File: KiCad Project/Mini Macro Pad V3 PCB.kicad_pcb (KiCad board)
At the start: 4 copper layers, 65 x 65 mm, 98 parts, among them J1 USB_C_Receptacle_USB2.0_14P, SW1 SW_Push bootsel, SW10 SW_Push, SW11 SW_Push, SW12 SW_Push, SW13 SW_Push, SW14 SW_Push, SW15 SW_Push, SW16 SW_Push, SW17 SW_Push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

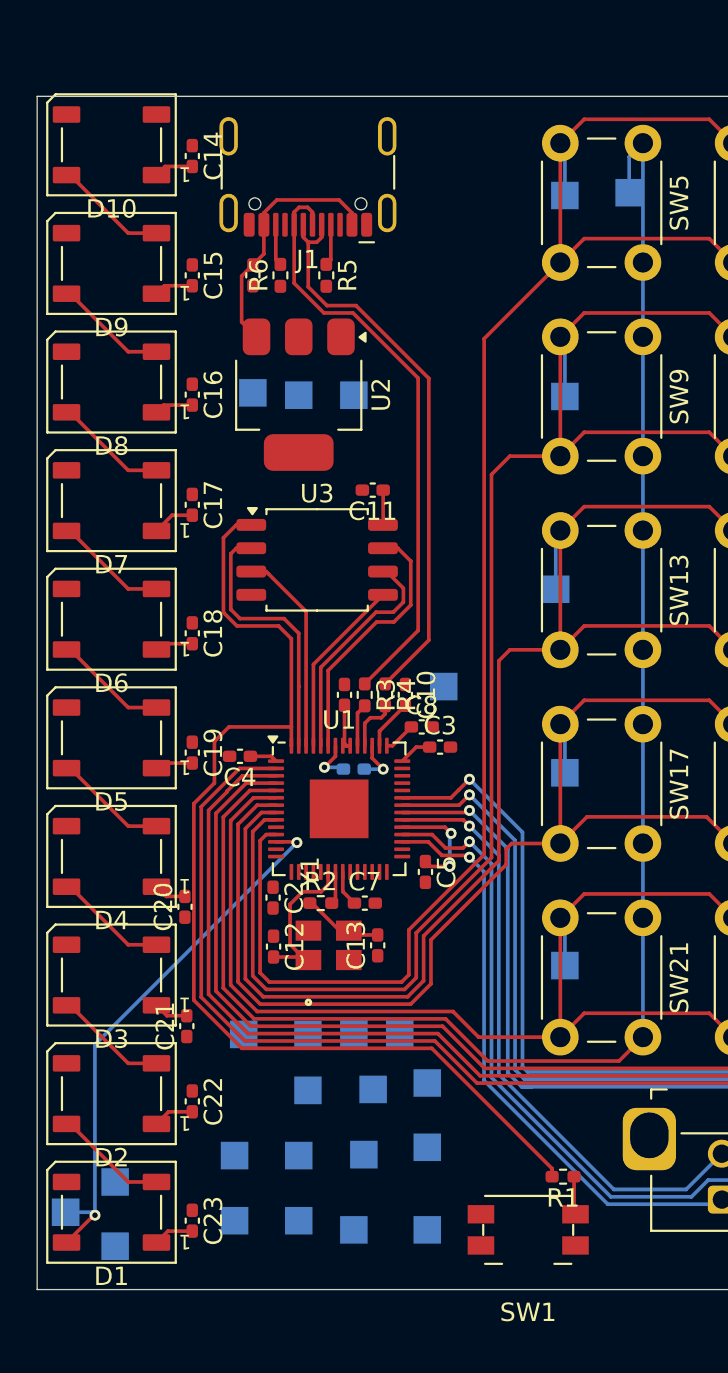
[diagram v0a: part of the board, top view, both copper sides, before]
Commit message: added vias to connect components to ground & power planes
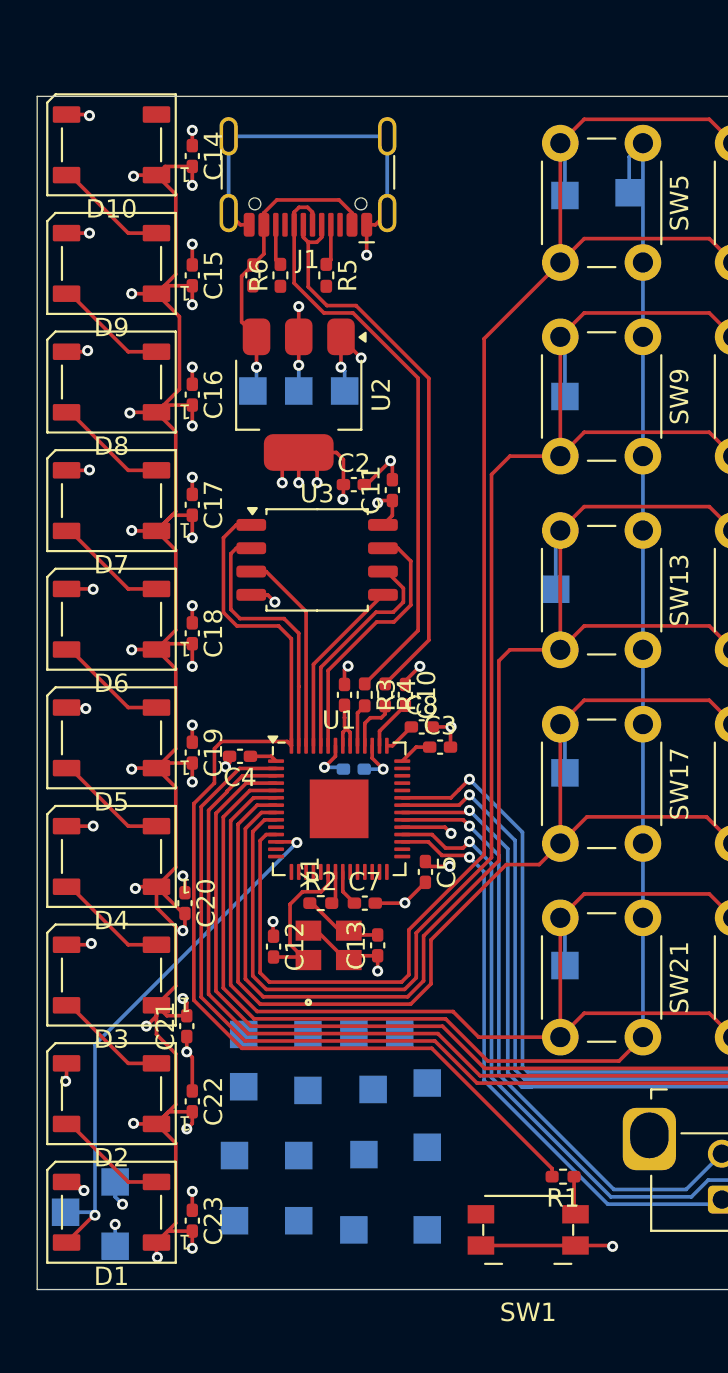
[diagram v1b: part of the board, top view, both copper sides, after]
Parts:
- moved TP14 24.4 mm to (114.0, 111.2)
- moved C2 22.9 mm to (120.0, 78.4), turned to 0 degrees
- moved C11 1.07 mm to (122.1, 78.7), turned to 90 degrees
- moved TP21 0.55 mm to (119.5, 73.3)
- moved TP20 0.23 mm to (117.0, 73.3)
- moved C20 0.20 mm to (110.8, 101.2), turned to -90 degrees
- moved TP22 0.10 mm to (114.5, 73.3)
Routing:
- net +3.3V: track 37.9 -> 143.2 mm, vias 2 -> 31
- net GND: track 0.00 -> 74.1 mm, vias 0 -> 32
- net VBUS: track 13.6 -> 16.7 mm, vias 0 -> 1

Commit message: more routing work
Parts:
- removed TP10, TP11, TP12, TP7, TP8, TP9: ~, TestPoint:TestPoint_Pad_1.5x1.5mm
- C9: moved to F.Cu
- moved TP16 31.3 mm to (123.2, 88.7), turned to -90 degrees
- moved TP15 27.2 mm to (120.5, 88.7), turned to -90 degrees
- moved TP14 22.8 mm to (117.7, 88.7), turned to -90 degrees
- moved TP13 19.7 mm to (115.0, 88.7), turned to -90 degrees
- moved TP5 15.6 mm to (113.2, 101.2), turned to -90 degrees
- moved TP6 15.4 mm to (113.2, 103.5), turned to -90 degrees
- moved TP4 14.8 mm to (113.2, 98.8), turned to -90 degrees
- moved TP3 13.6 mm to (113.2, 96.5), turned to -90 degrees
- moved TP1 5.11 mm to (123.7, 105.9), turned to 90 degrees
- moved TP2 4.95 mm to (123.7, 103.5), turned to 90 degrees
- moved C9 4.17 mm to (119.0, 89.9), turned to 90 degrees
- moved C8 1.00 mm to (124.7, 91.6)
- moved R3 0.61 mm to (121.2, 89.9)
- moved C10 0.61 mm to (123.4, 89.9)
- moved C6 0.61 mm to (120.1, 89.9)
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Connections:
- U1 pad 17: Net-(U1-GPIO14) -> unconnected-(U1-GPIO14-Pad17)
- U1 pad 18: Net-(U1-GPIO15) -> unconnected-(U1-GPIO15-Pad18)
- U1 pad 26: unconnected-(U1-RUN-Pad26) -> +3.3V
- U1 pad 27: Net-(U1-GPIO16) -> unconnected-(U1-GPIO16-Pad27)
- U1 pad 28: Net-(U1-GPIO17) -> unconnected-(U1-GPIO17-Pad28)
- U1 pad 29: Net-(U1-GPIO18) -> unconnected-(U1-GPIO18-Pad29)
- U1 pad 30: Net-(U1-GPIO19) -> unconnected-(U1-GPIO19-Pad30)
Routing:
- net Net-(U1-GPIO27_ADC1): track 0.00 -> 11.5 mm, vias 0 -> 1
- net Net-(U1-GPIO26_ADC0): track 0.00 -> 11.1 mm, vias 0 -> 1
- net Net-(U1-SWCLK): track 0.00 -> 10.9 mm, vias 0 -> 1
- net Net-(U1-SWD): track 0.00 -> 10.7 mm, vias 0 -> 1
- net Net-(U1-GPIO13): track 0.00 -> 9.97 mm, vias 0 -> 1
- net Net-(C9-Pad1): track 2.36 -> 11.4 mm, vias 1 -> 2
- net /NEOPIXEL_DIN: track 29.8 -> 38.7 mm
- net Net-(U1-GPIO28_ADC2): track 0.00 -> 6.78 mm, vias 0 -> 1
- net GND: track 74.1 -> 80.3 mm, vias 32 -> 35
- net Net-(U1-VREG_VOUT): track 2.56 -> 8.77 mm, vias 1 -> 2
- net Net-(U1-GPIO29_ADC3): track 0.00 -> 6.17 mm, vias 0 -> 1
- net Net-(U1-GPIO10): track 0.00 -> 6.06 mm, vias 0 -> 1
- net +3.3V: track 143.2 -> 147.7 mm, vias 31 -> 32
- net Net-(U1-GPIO12): track 0.00 -> 4.08 mm, vias 0 -> 1
- net /MATRIX_R1: track 131.0 -> 134.5 mm
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
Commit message: test
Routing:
- net (no net): track 0.00 -> 26.9 mm, vias 0 -> 2
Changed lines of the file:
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@@
 	)
 	(segment
+		(start 164.9 113)
+		(end 163.5 113)
+		(width 0.2)
+		(layer "F.Cu")
+		(net 0)
+	)
+	(segment
+		(start 136.55 113.4)
+		(end 136.1 113.85)
+		(width 0.2)
+		(layer "F.Cu")
+		(net 0)
+	)
+	(segment
+		(start 153.7 113)
+		(end 152.85 113.85)
+		(width 0.2)
+		(layer "F.Cu")
+		(net 0)
+	)
+	(segment
+		(start 148.95 113.85)
+		(end 149 113.85)
+		(width 0.2)
+		(layer "F.Cu")
+		(net 0)
+	)
+	(segment
+		(start 148.5 113.4)
+		(end 148.95 113.85)
+		(width 0.2)
+		(layer "F.Cu")
+		(net 0)
+	)
+	(segment
+		(start 146.8 113.4)
+		(end 136.55 113.4)
+		(width 0.2)
+		(layer "F.Cu")
+		(net 0)
+	)
+	(segment
+		(start 146.8 113.4)
+		(end 148.5 113.4)
+		(width 0.2)
+		(layer "F.Cu")
+		(net 0)
+	)
+	(segment
+		(start 165.75 113.85)
+		(end 164.9 113)
+		(width 0.2)
+		(layer "F.Cu")
+		(net 0)
+	)
+	(segment
+		(start 163.5 113)
+		(end 153.7 113)
+		(width 0.2)
+		(layer "F.Cu")
+		(net 0)
+	)
+	(via micro
+		(at 146.8 113.4)
+		(size 0.6)
+		(drill 0.3)
+		(layers "F.Cu" "In1.Cu")
+		(net 0)
+	)
+	(via micro
+		(at 163.5 113)
+		(size 0.6)
+		(drill 0.3)
+		(layers "F.Cu" "In1.Cu")
+		(net 0)
+	)
+	(segment
 		(start 105.794445 97.005555)
 		(end 105.8 97)
@@
 	)
 	(segment
-		(start 117.5765 112.7804)
-		(end 127.9196 112.7804)
-		(width 0.2)
-		(layer "F.Cu")
-		(net 58)
-	)
-	(segment
 		(start 112.407912 94.657888)
-		(end 111.285863 95.779937)
-		(width 0.2)
-		(layer "F.Cu")
-		(net 58)
-	)
-	(segment
-		(start 112.8 92.392088)
 		(end 112.407912 92.784176)
 		(width 0.2)
@@
 	)
 	(segment
-		(start 111.285863 106.489763)
-		(end 117.5765 112.7804)
+		(start 113.600001 80.595)
+		(end 112.898 81.297001)
 		(width 0.2)
 		(layer "F.Cu")
@@
 	)
 	(segment
-		(start 113.600001 80.595)
-		(end 112.898 81.297001)
+		(start 116.2011 111.405)
+		(end 111.285863 106.489763)
 		(width 0.2)
 		(layer "F.Cu")
@@
 	)
 	(segment
-		(start 127.9196 112.7804)
-		(end 130.8025 115.6633)
+		(start 130.8025 116.1)
+		(end 130.8025 115.7075)
 		(width 0.2)
 		(layer "F.Cu")
@@
 	)
 	(segment
-		(start 116.367088 92.392088)
-		(end 112.8 92.392088)
+		(start 111.285863 95.779937)
+		(end 112.407912 94.657888)
 		(width 0.2)
 		(layer "F.Cu")
@@
 	(segment
 		(start 112.407912 92.784176)
-		(end 112.407912 94.657888)
+		(end 112.8 92.392088)
 		(width 0.2)
 		(layer "F.Cu")
@@
 	)
 	(segment
-		(start 116.6 92.625)
-		(end 116.367088 92.392088)
+		(start 111.285863 106.489763)
+		(end 111.285863 95.779937)
 		(width 0.2)
 		(layer "F.Cu")
@@
 	)
 	(segment
-		(start 111.285863 95.779937)
-		(end 111.285863 106.489763)
+		(start 116.367088 92.392088)
+		(end 116.6 92.625)
 		(width 0.2)
 		(layer "F.Cu")
@@
 	)
 	(segment
+		(start 126.5 111.405)
+		(end 116.2011 111.405)
+		(width 0.2)
+		(layer "F.Cu")
+		(net 58)
+	)
+	(segment
 		(start 113.7339 87.201)
 		(end 115.5339 87.201)
@@
 	)
 	(segment
-		(start 130.8025 115.6633)
-		(end 130.8025 116.1)
+		(start 112.8 92.392088)
+		(end 116.367088 92.392088)
 		(width 0.2)
 		(layer "F.Cu")
@@
 		(net 58)
 	)
+	(segment
+		(start 130.8025 115.7075)
+		(end 126.5 111.405)
+		(width 0.2)
+		(layer "F.Cu")
+		(net 58)
+	)
+	(zone
+		(net 0)
+		(net_name "")
+		(layer "F.Cu")
+		(name "$teardrop_padvia$")
+		(hatch none 0.1)
+		(priority 30000)
+		(attr
+			(teardrop
+				(type padvia)
+			)
+		)
+		(connect_pads yes
+			(clearance 0)
+		)
+		(min_thickness 0.0254)
+		(filled_areas_thickness no)
+		(fill yes
+			(thermal_gap 0.5)
+			(thermal_bridge_width 0.5)
+			(island_removal_mode 1)
+			(island_area_min 10)
+		)
+		(polygon
+			(pts
+				(xy 138.55 113.5) (xy 138.55 113.3) (xy 137.363555 112.601115) (xy 136.099 113.85) (xy 137.55 114.600312)
+			)
+		)
+	)
 	(zone

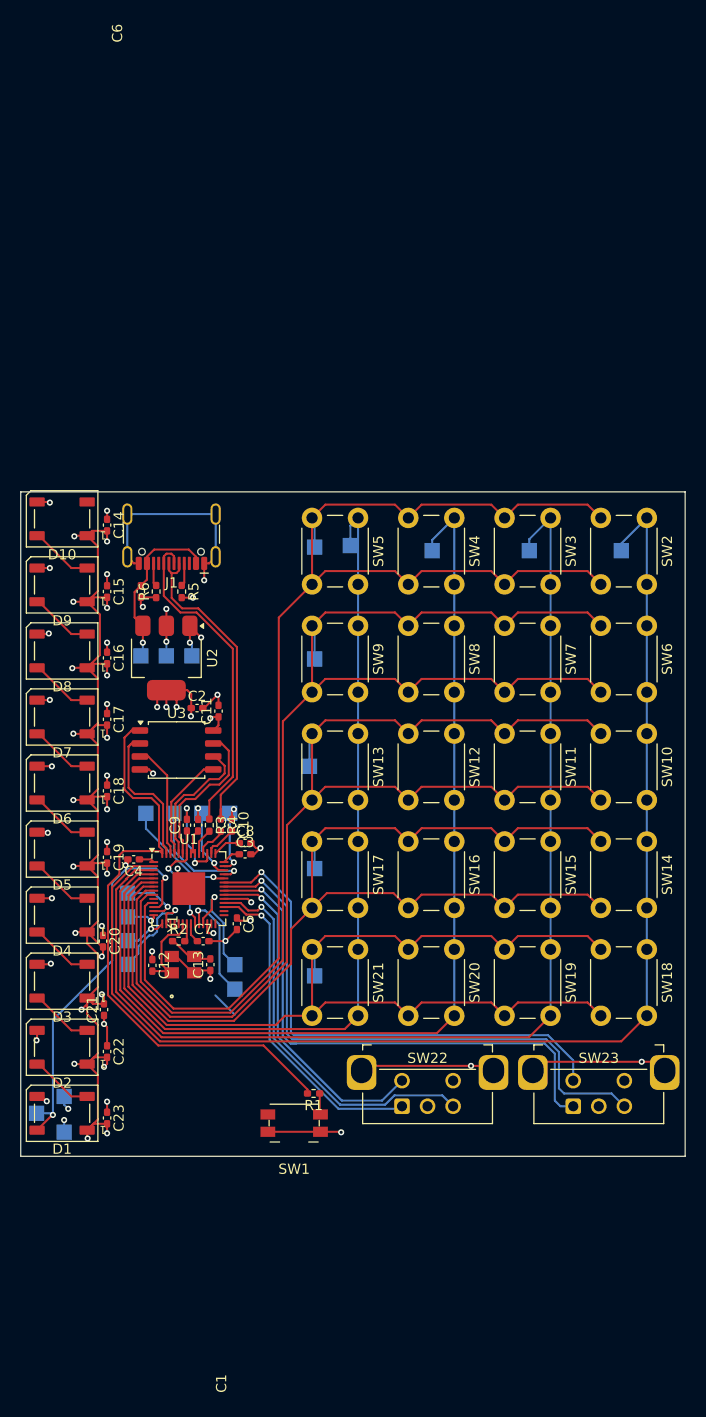
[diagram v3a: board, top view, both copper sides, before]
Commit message: tweaks for DRC
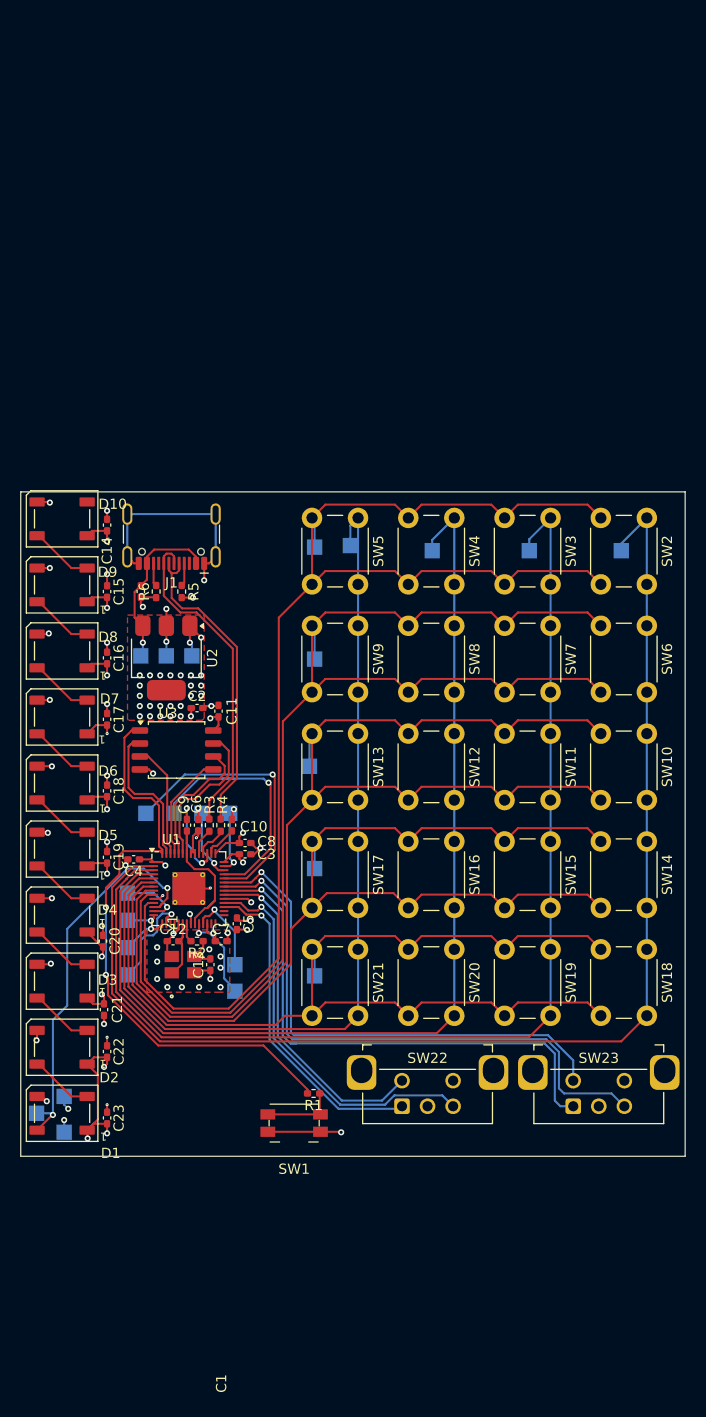
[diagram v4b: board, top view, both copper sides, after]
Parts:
- U1: footprint Package_DFN_QFN:QFN-56-1EP_7x7mm_P0.4mm_EP3.2x3.2mm -> Package_DFN_QFN:QFN-56-1EP_7x7mm_P0.4mm_EP3.2x3.2mm_ThermalVias
- U2: value NCP1117-3.3_SOT223 -> NCP1117
- moved C12 3.12 mm to (117.7, 101.2), turned to 0 degrees
- moved R2 1.80 mm to (120.0, 101.2), turned to 180 degrees
- moved C7 1.75 mm to (122.4, 101.2)
- moved TP6 1.03 mm to (113.2, 104.5)
- moved TP5 0.68 mm to (113.2, 101.8), turned to 90 degrees
- moved TP4 0.34 mm to (113.2, 99.2)
- moved TP1 0.20 mm to (123.7, 106.1), turned to -90 degrees
- turned TP13 to 0 degrees
- turned TP14 to 180 degrees
- turned TP15 to 0 degrees
- turned TP16 to 180 degrees
- turned TP23 to -90 degrees
- turned TP24 to -90 degrees
- turned TP25 to -90 degrees
- turned TP26 to -90 degrees
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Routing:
- net +3.3V: track 147.7 -> 70.4 mm, vias 32 -> 49
- net (no net): track 26.9 -> 0.00 mm, vias 2 -> 0
- net Net-(U1-GPIO26_ADC0): track 11.1 -> 27.6 mm
- net Net-(U1-GPIO27_ADC1): track 11.5 -> 24.6 mm
- net Net-(R1-Pad1): track 1.97 -> 7.12 mm
- net GND: track 80.3 -> 75.4 mm, vias 35 -> 47
- net /XIN: track 8.34 -> 5.44 mm
- net Net-(U1-SWD): track 10.7 -> 8.30 mm
- net Net-(U1-SWCLK): track 10.9 -> 8.54 mm
- net Net-(C9-Pad1): track 11.4 -> 13.0 mm, vias 2 -> 0
- net /MATRIX_C4: track 90.5 -> 89.5 mm
- net /USB_D-: track 31.9 -> 30.9 mm
- net /QSPI_SS: track 58.1 -> 58.2 mm, vias 0 -> 2
- added copper zone on F.Cu, net +3.3V
- added copper zone on F.Cu, net GND

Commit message: added silkscreen things
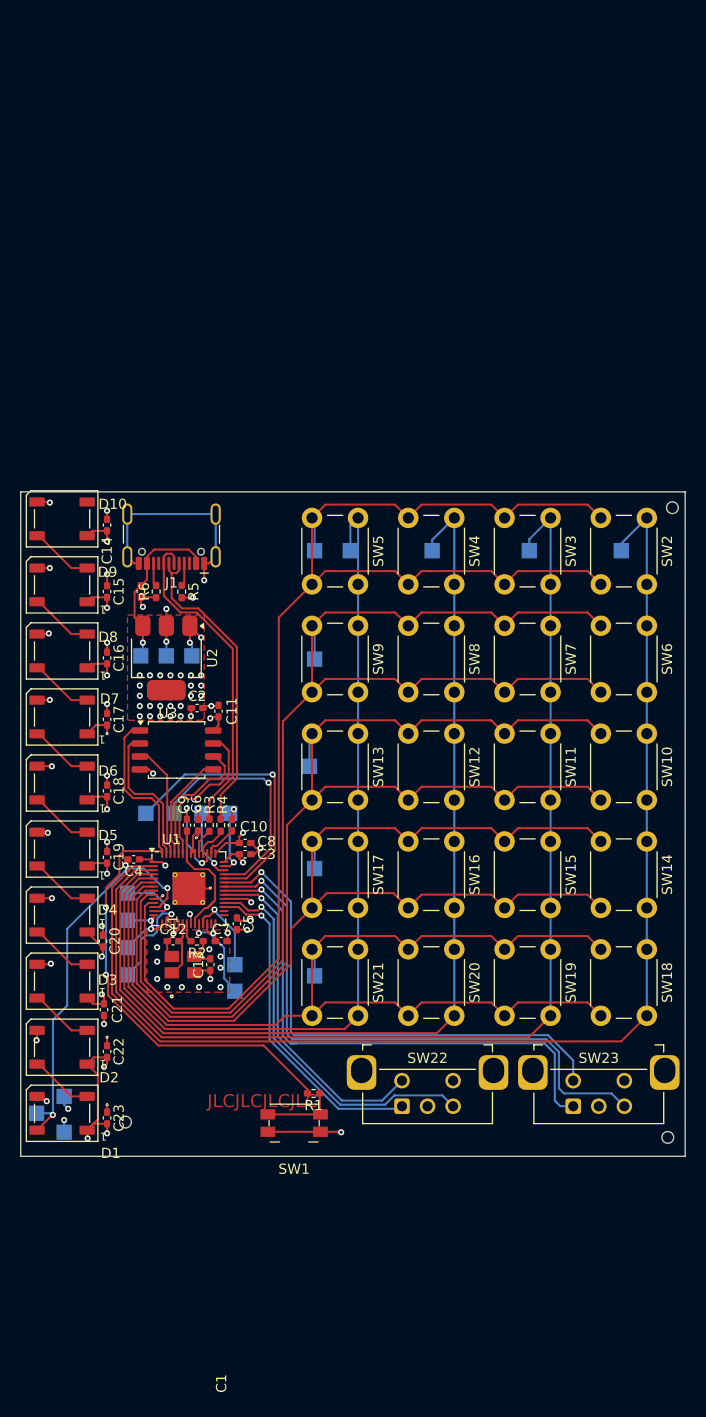
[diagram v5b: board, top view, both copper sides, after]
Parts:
- added H1: MountingHole, MountingHole:ToolingHole_1.152mm, F.Cu at (166.5, 58.8)
- added H2: MountingHole, MountingHole:ToolingHole_1.152mm, F.Cu at (113.0, 118.9)
- added H3: MountingHole, MountingHole:ToolingHole_1.152mm, F.Cu at (166.1, 120.4)
- U2: value NCP1117 -> NCP1117-3.3_SOT223
- moved TP28 0.50 mm to (135.0, 63.0)
- moved TP23 0.35 mm to (131.5, 63.0)
- turned TP18 to 90 degrees
- turned TP19 to 90 degrees
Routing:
- net Net-(U1-GPIO27_ADC1): track 24.6 -> 23.5 mm
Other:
- board text added: "Designed by Gavin Strand 9195874@gmail.com"
- board text added: "JLCJLCJLCJLC"
- board text added: "Mini Macro Pad V3"
- board text added: "REV 1.0"

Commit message: moved USB C port to the right more
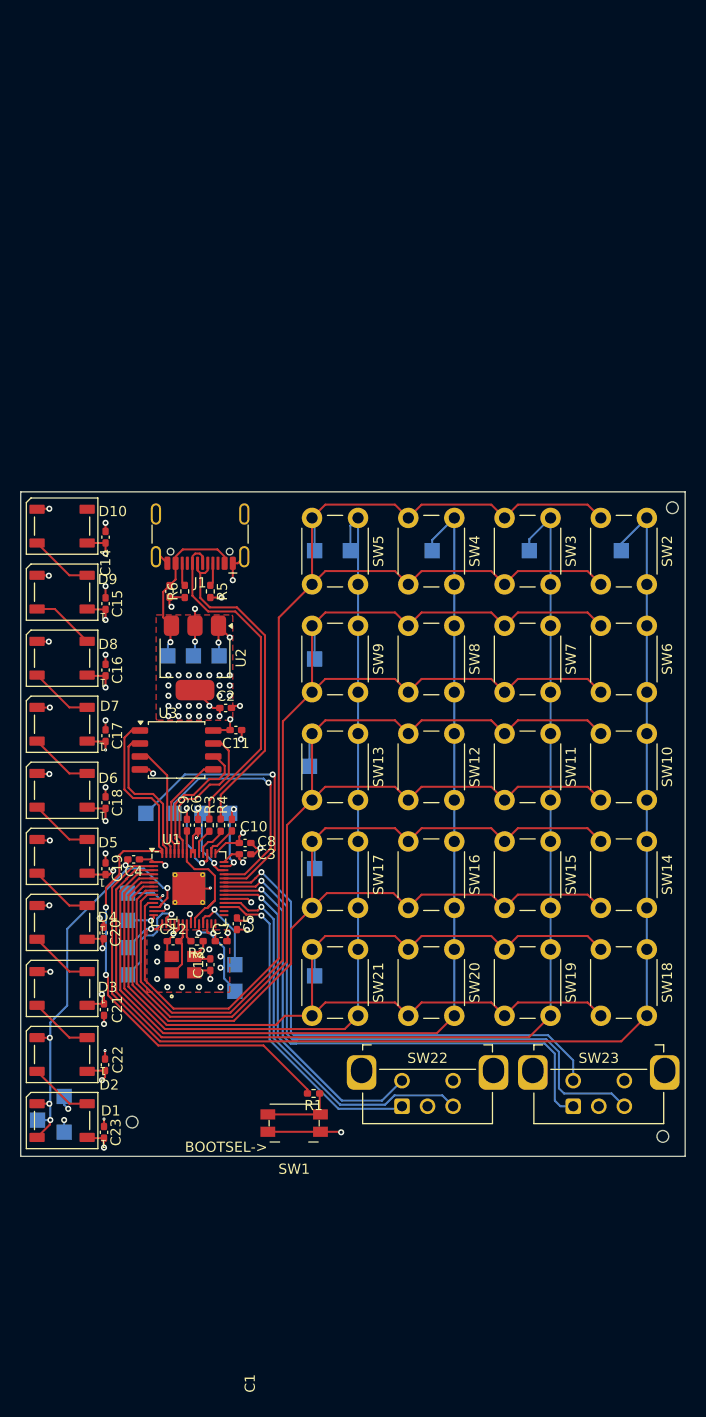
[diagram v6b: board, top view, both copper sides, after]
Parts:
- SW1: value SW_Push bootsel -> BOOTSEL->
- moved C1 2.80 mm to (117.3, 67.0)
- moved C2 2.80 mm to (122.8, 78.4)
- moved J1 2.80 mm to (120.3, 60.5)
- moved R5 2.80 mm to (121.3, 67.0)
- moved R6 2.80 mm to (118.8, 67.0)
- moved U2 2.80 mm to (119.8, 73.5)
- moved TP20 2.65 mm to (119.7, 73.3)
- moved TP21 2.65 mm to (122.2, 73.3)
- moved TP22 2.65 mm to (117.2, 73.3)
- moved C11 2.51 mm to (123.8, 80.5), turned to 0 degrees
- moved C17 1.61 mm to (111.0, 81.1)
- moved C23 1.43 mm to (110.9, 119.9)
- moved C22 1.32 mm to (111.0, 113.3)
- moved C15 1.19 mm to (111.0, 68.2)
- moved C16 1.19 mm to (111.0, 74.7)
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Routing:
- net GND: track 75.4 -> 58.1 mm, vias 47 -> 48
- net +3.3V: track 70.4 -> 61.8 mm, vias 49 -> 48
- net /USB_D-: track 30.9 -> 31.9 mm
- net /USB_D+: track 32.3 -> 33.3 mm
- net VBUS: track 16.4 -> 15.4 mm

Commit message: small tweaks before ordering first prototype
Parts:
- added TP7: ~, TestPoint:TestPoint_Pad_1.5x1.5mm, B.Cu at (124.2, 67.4)
- added TP8: ~, TestPoint:TestPoint_Pad_1.5x1.5mm, B.Cu at (126.8, 67.4)
- SW1: value BOOTSEL-> -> SW_Push bootsel
- moved TP19 0.44 mm to (107.0, 116.0)
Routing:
- net /USB_D+: track 33.3 -> 38.7 mm, vias 0 -> 1
- net /USB_D-: track 31.9 -> 34.2 mm, vias 0 -> 1
- net /NEOPIXEL_DIN: track 38.7 -> 37.6 mm
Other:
- board text added: "BOOTSEL->"
